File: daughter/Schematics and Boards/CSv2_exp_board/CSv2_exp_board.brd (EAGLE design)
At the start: 38.1 x 43.8 mm, 130 parts, among them J1 HIROSE-DF40_44-PIN_CONNECTORS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, J2 J-SERIAL-PORT, J3 CORTEX_DEBUG_SMD, J301 HIROSE-DF40_44-PIN_CONNECTORS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, J4 SJ-43514-SMT, J7 J-USB-HIROSE-MICRO-USB, SW1 SPST_TACT-KMR2, SW2 SPST_TACT-KMR2, U1 LOADSWITCH-MIC94164, U10 LOADSWITCH-MIC94164, U11 BMI160, U12 TLV320DAC26IRHB, U13 ADG839YKSZ-500RL7KS_6_ADI-L, U14 LOADSWITCH-MIC94164, U2 ADA4841-1YRJZ-R7, U205 MPL3115A2, U3 Value, U4 RFM69HCW, U5 Value, U6 Value, U7 LOADSWITCH-MIC94164, U8 LOADSWITCH-MIC94164, U9 LOADSWITCH-MIC94164, X1 32.768kHz, X2 32.768, X3 uFL, X4 uFL, X5 uFL, X6 uFL

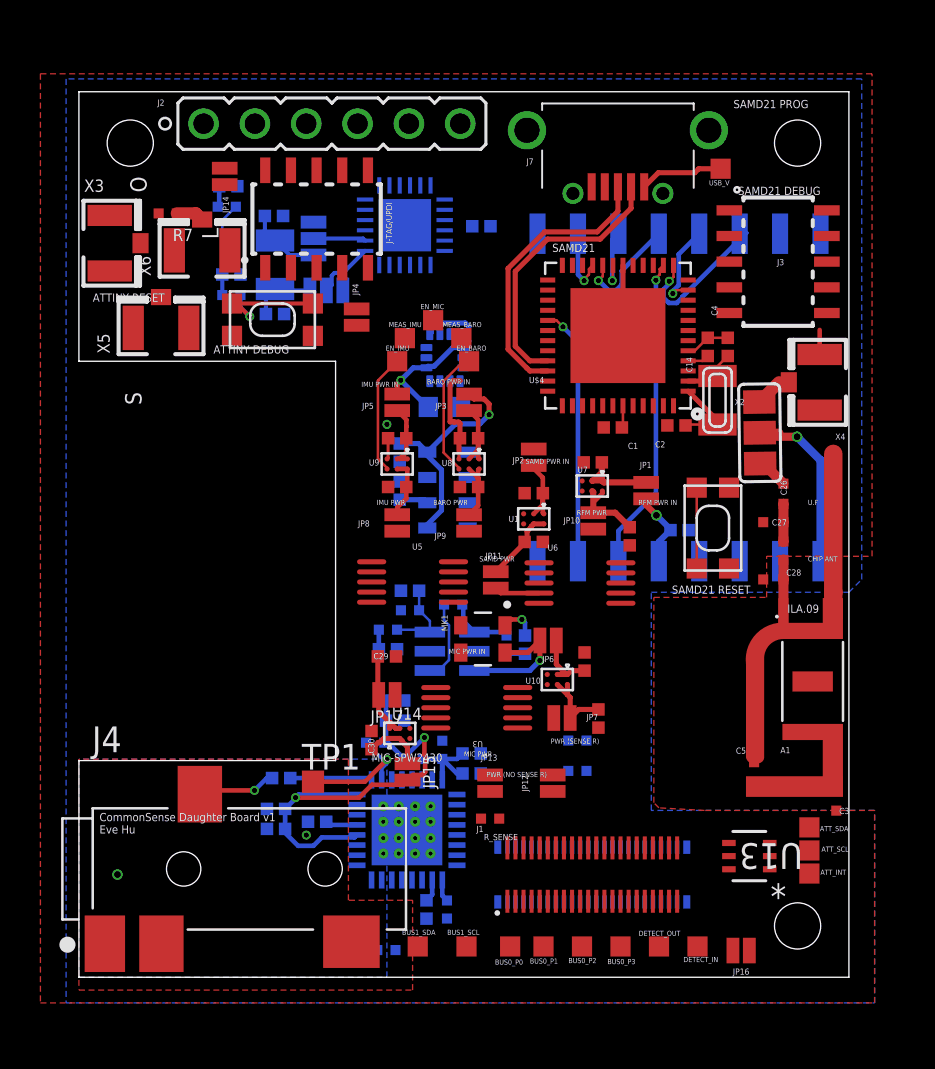
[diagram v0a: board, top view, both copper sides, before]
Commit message: DTR-moved the chip antenna a bit further from the connector
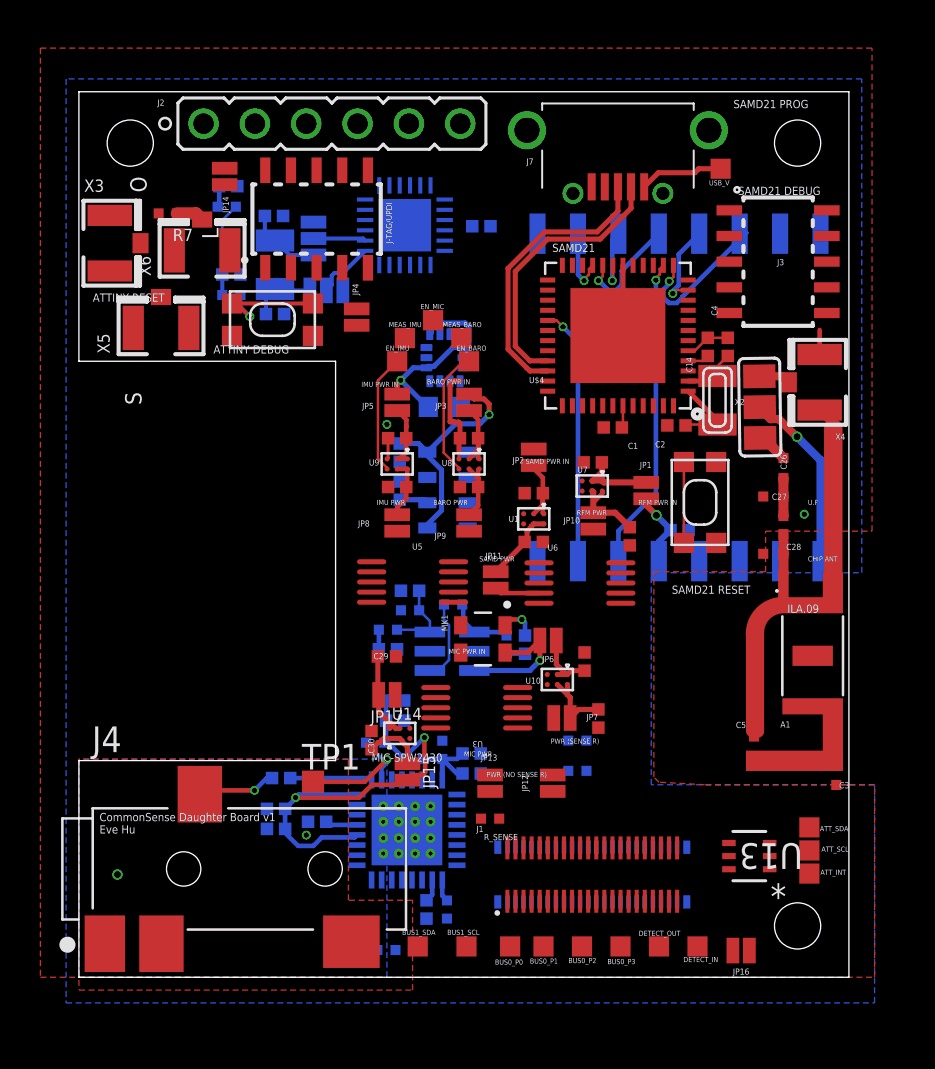
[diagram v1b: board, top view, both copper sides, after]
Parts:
- moved SW2 1.42 mm to (30.7, 23.5)
- moved C26 1.27 mm to (34.9, 25.2)
- moved L1 1.27 mm to (34.9, 22.4)
- moved A1 1.27 mm to (36.3, 15.9)
- moved C27 1.27 mm to (34.4, 23.8)
- moved C28 1.27 mm to (34.4, 21.0)
- moved C3 1.27 mm to (37.5, 10.0)
- moved C5 1.27 mm to (33.4, 11.4)
- moved SJ3 1.27 mm to (33.7, 28.2)
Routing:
- net GND: track 32.3 -> 39.1 mm, vias 1 -> 2
- added copper zone on layer 15, net B

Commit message: DTR-fixed keepout error
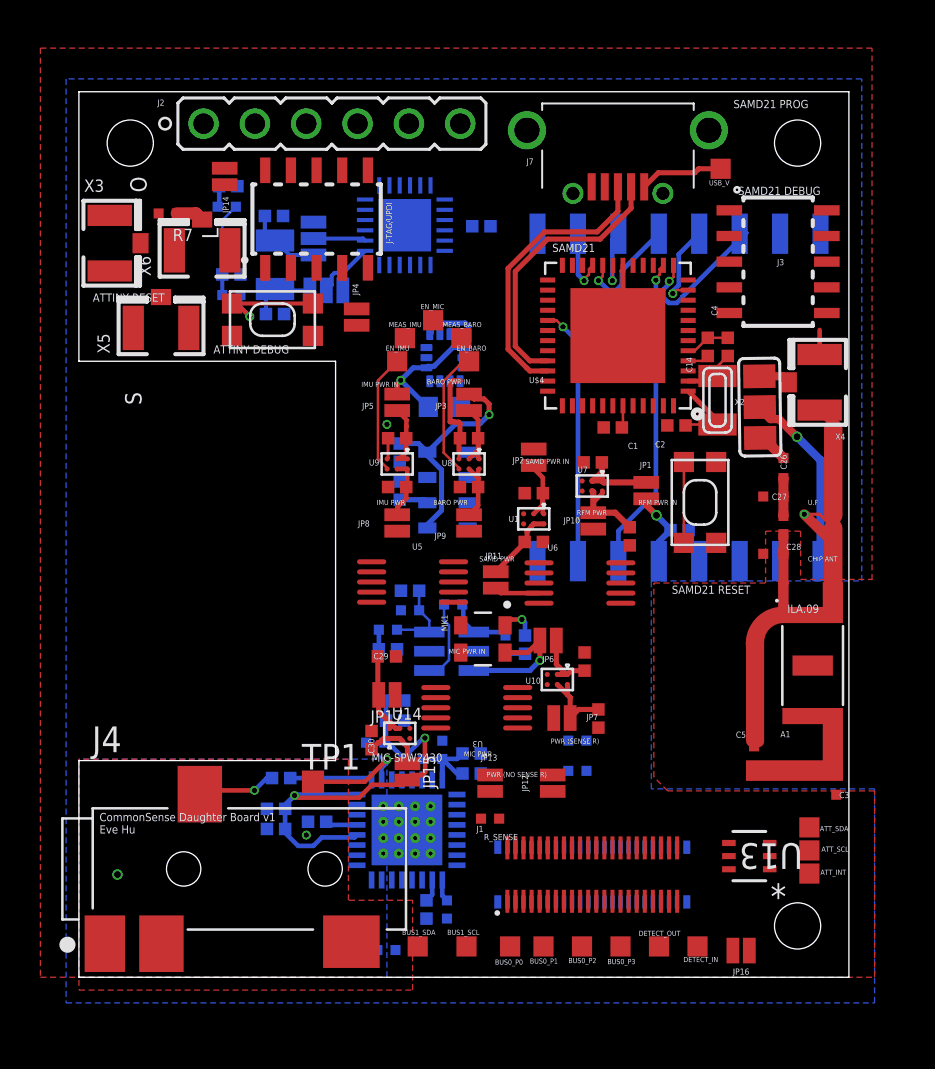
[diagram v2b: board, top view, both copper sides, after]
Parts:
- moved A1 0.48 mm to (36.3, 15.4)
- moved C3 0.48 mm to (37.5, 9.53)
- moved C5 0.48 mm to (33.4, 10.9)
- moved R1 0.05 mm to (21.1, 16.5)
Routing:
- net GND: track 39.1 -> 45.3 mm
- net N$4: track 0.00 -> 4.23 mm

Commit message: DTR-added ldo and 80% manual routing
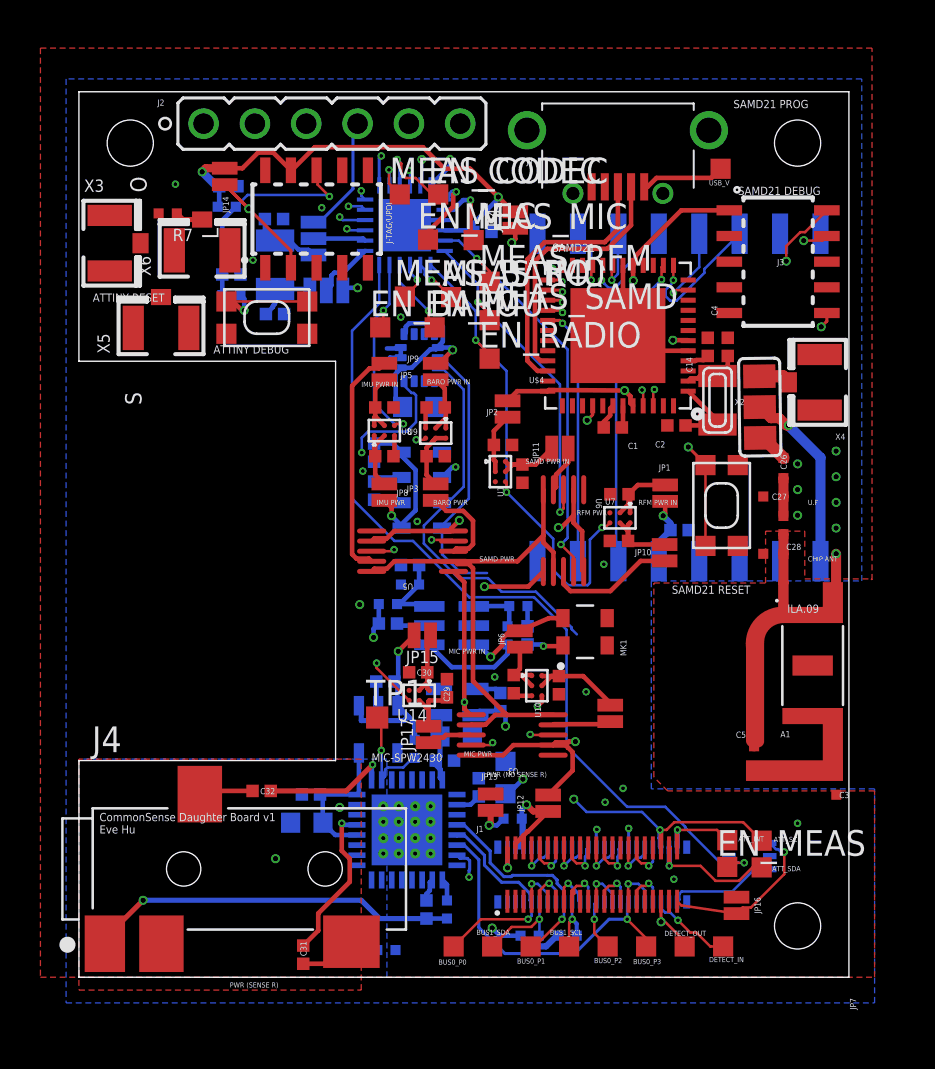
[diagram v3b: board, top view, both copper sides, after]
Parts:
- removed R10, R9: 100k, Resistors:R0402
- added C41, C42: 2.2u, Capacitors:C0402
- added EN_CODEC, EN_MEAS, EN_RADIO, MEAS_CODEC, MEAS_MIC, MEAS_RFM, MEAS_SAMD: TPTP10SQ, TestPoints:TP10SQ
- added U15: LP2980AIM5-2.5/NOPBMF05A_TEX-L, CommonSense-DTR-v1:MF05A_TEX-L
- added U16: NCP553SQ18T1GSC-82AB_ONS-L, CommonSense-DTR-v1:SC-82AB_ONS-L
- C35, C37, C39: device Capacitors:C0402 -> Capacitors:C0603
- moved R5 9.94 mm to (22.3, 2.06)
- moved JP4 9.20 mm to (21.6, 37.5)
- moved JP9 8.59 mm to (15.1, 30.0), turned to 270 degrees
- moved R6 8.17 mm to (24.2, 2.06)
- moved JP11 7.24 mm to (23.8, 26.2), turned to 180 degrees
- moved JP15 6.80 mm to (17.0, 16.9), turned to 180 degrees
- moved C35 6.66 mm to (21.1, 9.88), turned to 90 degrees
- moved C31 6.61 mm to (11.1, 1.12), flipped to the top, turned to 270 degrees
- moved JP3 6.11 mm to (15.1, 24.0), turned to 270 degrees
- moved C19 5.75 mm to (15.1, 28.2), turned to 0 degrees
- moved C34 5.30 mm to (19.8, 9.40), turned to 90 degrees
- moved BUS1_SCL 5.08 mm to (24.3, 1.52)
- moved MK1 5.07 mm to (25.0, 17.1), turned to 90 degrees
- moved EN_BARO 4.70 mm to (14.9, 32.2)
- moved U8 4.50 mm to (15.1, 27.1), turned to 90 degrees
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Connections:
- net N$14 renamed MICBIAS
- net N$16 renamed HPR
- net N$28 renamed MICIN
- removed net N$21: C38.1, C39.1, R10.1, R9.1, U12.32
- new net +1V8_CODEC: C38.1, C39.1, U12.32, U16.3
- new net +3V_CODEC_A: C36.1, C37.1, U12.20, U12.24, U15.5
- new net HPL: C31.2, J4.2
- net +3V3_CODEC: now also C41.1, C42.1, U15.1, U15.3, U16.2; no longer C36.1, C37.1, R9.2, U12.20, U12.24
- net AGND: no longer C31.2, J4.2
- net EN_BARO: now also ATTINY-817.11; no longer ATTINY-817.5
- net EN_CODEC: now also EN_CODEC.TP
- net EN_IMU: now also ATTINY-817.10; no longer ATTINY-817.2
- net EN_MEAS: now also EN_MEAS.TP
- net EN_RADIO: now also ATTINY-817.7, EN_RADIO.TP; no longer ATTINY-817.6
- net GND: now also ATTINY-817.25, C41.2, C42.2, U15.2, U16.1; no longer R10.2
- net MEAS_CODEC: now also MEAS_CODEC.TP
- net MEAS_MIC: now also ATTINY-817.2, MEAS_MIC.TP; no longer ATTINY-817.7
- net MEAS_RFM: now also ATTINY-817.5, MEAS_RFM.TP; no longer ATTINY-817.11
- net MEAS_SAMD: now also ATTINY-817.6, MEAS_SAMD.TP; no longer ATTINY-817.10
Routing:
- net DTR_DETECT_OUT: track 0.00 -> 59.6 mm, vias 0 -> 2
- net MASTER_I2C_SCL: track 0.00 -> 49.4 mm, vias 0 -> 3
- net BUS0_SERCOM_P3: track 0.00 -> 49.4 mm, vias 0 -> 2
- net BUS0_SERCOM_P0: track 0.00 -> 47.1 mm, vias 0 -> 3
- net BUS0_SERCOM_P1: track 0.00 -> 47.0 mm, vias 0 -> 3
- net +3V3_DTR0: track 0.00 -> 45.1 mm, vias 0 -> 3
- net EN_MEAS: track 0.00 -> 43.6 mm, vias 0 -> 1
- net ATT_INT: track 0.00 -> 38.5 mm, vias 0 -> 2
- net MEAS_CODEC: track 0.00 -> 36.4 mm, vias 0 -> 2
- net BUS0_SERCOM_P2: track 0.00 -> 36.0 mm, vias 0 -> 3
- net +3V3_NMEAS: track 0.00 -> 35.4 mm, vias 0 -> 3
- net EN_CODEC: track 0.00 -> 32.7 mm, vias 0 -> 2
- net MEAS_MIC: track 0.00 -> 32.4 mm, vias 0 -> 2
- net +3V3_DTR: track 0.00 -> 32.0 mm, vias 0 -> 3
- net EN_MIC: track 0.00 -> 31.9 mm, vias 0 -> 2
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
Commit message: DTR-drc resolved, schematic check, routing  check
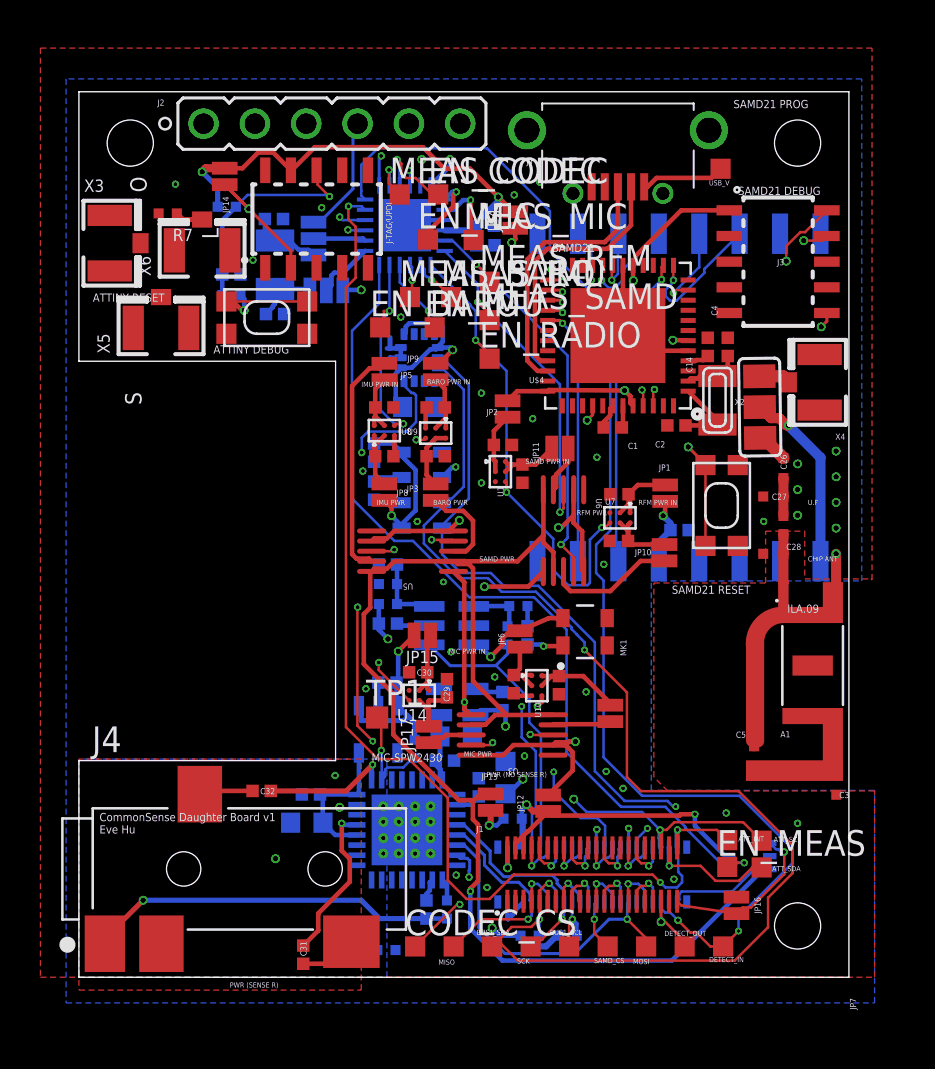
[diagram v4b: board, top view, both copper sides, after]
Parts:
- added CODEC_CS: TPTP10SQ, TestPoints:TP10SQ
- moved C12 13.1 mm to (20.1, 36.2)
- moved C42 5.87 mm to (21.0, 13.7), turned to 90 degrees
- moved C41 5.67 mm to (15.3, 14.6), turned to 0 degrees
- moved C8 1.09 mm to (15.3, 20.4)
- moved R3 1.09 mm to (15.3, 19.5)
- moved C13 0.33 mm to (20.1, 37.2)
- moved MEAS_BARO 0.26 mm to (16.4, 33.7)
- renumbered BUS0_P0 to MISO, BUS0_P1 to SCK, BUS0_P2 to SAMD_CS, BUS0_P3 to MOSI
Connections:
- net BUS0_GPIO1: now also CODEC_CS.TP
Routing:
- net DTR_DETECT_IN: track 17.8 -> 63.1 mm
- net +3V3_MEAS: track 26.8 -> 65.8 mm, vias 0 -> 1
- net BUS1_SERCOM_P0: track 24.4 -> 61.4 mm, vias 1 -> 2
- net MASTER_I2C_SDA: track 27.2 -> 57.0 mm, vias 3 -> 4
- net BUS1_SERCOM_P1: track 16.8 -> 45.7 mm, vias 1 -> 2
- net BUS1_GPIO1: track 12.5 -> 36.2 mm, vias 1 -> 2
- net ATT_INT: track 38.5 -> 56.7 mm, vias 2 -> 3
- net BUS0_AIN0: track 24.8 -> 40.0 mm, vias 1 -> 3
- net +3V3_DTR: track 32.0 -> 42.2 mm, vias 3 -> 4
- net BUS1_AIN0: track 5.07 -> 14.9 mm
- net BUS1_GPIO0: track 18.2 -> 23.5 mm, vias 1 -> 2
- net BUS0_GPIO1: track 11.9 -> 16.5 mm, vias 2 -> 3
- net GND: track 38.5 -> 42.2 mm, vias 18 -> 32
- net HPL: track 3.82 -> 2.84 mm
- net BUS0_SERCOM_P1: track 47.0 -> 46.1 mm
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
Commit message: DTR-filled in device specs and double checked the footprint consistency
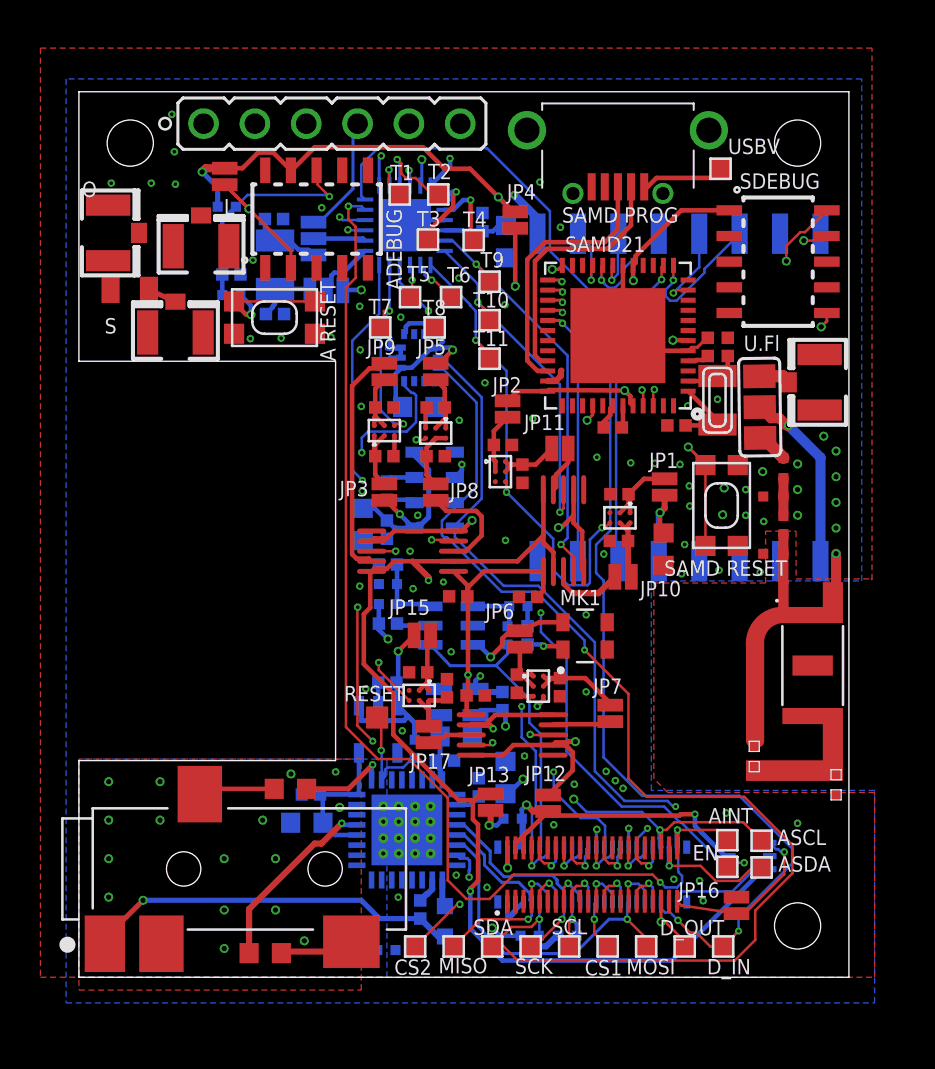
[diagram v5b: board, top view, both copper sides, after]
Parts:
- added C40: 10u, Capacitors:C0603
- added C43, C44, C45: 0.1u, Capacitors:C0402
- A1: device CommonSense-DTR-v1:ILA_09_CHIP_ANTENNA2 -> CommonSense-DTR-v1:ILA_09_CHIP_ANTENNA
- C1, C14: value 1uF -> 1u
- C11, C18, C20, C22, C24, C30: value 100n -> 0.1u
- C12: value 4.7nF -> 4.7u; device Capacitors:C0402 -> Capacitors:C0603
- C13: value 100nF -> 0.1u
- C2, C4: value 22pF -> 5.5p
- C203, C204, C25: value 0.1uF -> 0.1u
- C26: value (none) -> 22p
- C31, C32: value (none) -> 47u; device Capacitors:C0402 -> Capacitors:C0603
- C33: value (none) -> 0.1u
- C42: value 2.2u -> 1u
- C6: value 4.7u -> 0.68u
- C9: value 10uF -> 10u; device Capacitors:C0402 -> Capacitors:C0603
- J-TAG/UPDI: value ATTINY_AVR_DEBUG_SMD -> ATTINY_AVR_DEBUG; device CommonSense-DTR-v1:ATTINY_AVR_DEBUG -> CommonSense-DTR-v1:SAMTECH_FTSH-105-01
- L1: value L0402 -> 1.2n
- MK1: device SPW2430HR5H-B:MIC_SPW2430HR5H-B -> CommonSense-DTR-v1:MIC_SPW2430HR5H-B
- R1: value 1.5k -> 4.99k
- R2: value 100k -> 82.5k
- R27, R28: value (none) -> 0
- R3, R4: value 10k -> 100k
- R7: value (none) -> 50; device Resistors:R0402 -> Resistors:R0805
- R8: value (none) -> 2.2k; device Resistors:R0402 -> Resistors:R0603
- SW1, SW2: device adafruit:KMR2 -> CommonSense-DTR-v1:KMR2
- U2: value ADA4841-1YRJZ-R7 -> ADA4841-1YRJZ-R7RJ_6-L; device ADA1484:RJ_6 -> CommonSense-DTR-v1:RJ_6-L
- moved X5 4.50 mm to (6.05, 36.2)
- moved X6 4.27 mm to (4.78, 31.9)
- moved R7 4.23 mm to (2.51, 34.0)
- moved C203 3.86 mm to (15.2, 22.1)
- moved JP10 2.38 mm to (26.9, 19.8), turned to 0 degrees
- moved C31 1.88 mm to (9.22, 1.19), turned to 0 degrees
- moved C32 1.43 mm to (10.5, 9.32)
- moved C9 1.23 mm to (28.9, 21.2), flipped to the top, turned to 270 degrees
- moved C12 1.03 mm to (21.1, 36.4), turned to 90 degrees
- moved U205 0.64 mm to (17.6, 24.1)
- moved C204 0.63 mm to (15.2, 24.1)
- moved R8 0.59 mm to (18.1, 2.77)
- moved X3 0.51 mm to (1.45, 36.8)
- moved SW1 0.38 mm to (9.68, 32.6)
- moved JP1 0.31 mm to (29.0, 24.3)
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- renumbered ATT_INT to AINT, ATT_SCL to ASCL, ATT_SDA to ASDA, BUS1_SCL to SCL, BUS1_SDA to SDA, C27 to R27, C28 to R28, C3-4.7N to C46, CODEC_CS to CS2, DETECT_IN to D_IN, DETECT_OUT to D_OUT, EN_BARO to T7, EN_CODEC to T2, EN_IMU to T8, EN_MEAS to EN, EN_MIC to T3, EN_RADIO to T11, MEAS_BARO to T5, MEAS_CODEC to T1, MEAS_IMU to T6, MEAS_MIC to T4, MEAS_RFM to T9, MEAS_SAMD to T10, R1-100K to R10, R3-39R to R9, SAMD_CS to CS1, TP1 to RESET, USB_V to USBV
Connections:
- net +3V3_BARO: now also C40.2
- net +3V3_DTR: now also C43.1, C44.1, C45.1
- net GND: now also C40.1, C43.2, C44.2, C45.2, J3.9
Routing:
- net GND: track 42.2 -> 47.5 mm, vias 32 -> 73
- net +3V3_RFM_PWR: track 6.38 -> 3.68 mm
- net +3V3_MEAS: track 65.8 -> 68.3 mm, vias 1 -> 3
- net +3V3_DTR: track 42.2 -> 39.9 mm, vias 4 -> 3
- net +3V3_BARO: track 7.58 -> 9.44 mm
- net N$25: track 6.34 -> 4.53 mm
- net N$15: track 7.95 -> 9.31 mm
- net HPR: track 2.68 -> 3.79 mm
- net BUS1_SERCOM_P1: track 45.7 -> 44.6 mm
- net EN_MEAS: track 43.8 -> 42.7 mm, vias 1 -> 3
- net +3V3_RFM: track 3.39 -> 4.46 mm
- net HPL: track 2.84 -> 3.90 mm
- net BUS1_SERCOM_P0: track 61.4 -> 60.5 mm
- net N$12: track 5.58 -> 6.39 mm
- net +3V3_IMU_PWR: track 4.54 -> 5.26 mm
- removed copper zone on layer 15, net B
- removed copper zone on layer 2, net T
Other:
- board text added: "A RESET"
- board text added: "ADEBUG"
- board text added: "ATTINY817"
- board text added: "CommonSense Daughter Board v1 Eve Hu 06/29/2020"
- board text added: "IMU"
- board text added: "SAMD PROG"
- board text added: "SAMD RESET"
- board text added: "SDEBUG"
- board text removed: "ATTINY DEBUG"
- board text removed: "ATTINY RESET"
- board text removed: "ATTINY-817"
- board text removed: "BARO PWR"
- board text removed: "BARO PWR IN"
- board text removed: "CHIP ANT"
- board text removed: "CommonSense Daughter Board v1 Eve Hu"
- board text removed: "ILA.09"
- board text removed: "IMU PWR"
- board text removed: "IMU PWR IN"
- board text removed: "IMU-BMI160"
- board text removed: "MIC PWR"
- board text removed: "MIC PWR IN"
- board text removed: "MIC-SPW2430"
- board text removed: "PWR (NO SENSE R)"
- board text removed: "PWR (SENSE R)"
- board text removed: "RFM PWR"
- board text removed: "RFM PWR IN"
- board text removed: "SAMD PWR"
- board text removed: "SAMD PWR IN"
- board text removed: "SAMD21 DEBUG"
- board text removed: "SAMD21 PROG"
- board text removed: "SAMD21 RESET"
